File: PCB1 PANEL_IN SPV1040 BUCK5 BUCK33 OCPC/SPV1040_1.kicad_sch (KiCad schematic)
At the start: 14 parts, among them J2 SOLAR, U2 SPV1040TTR

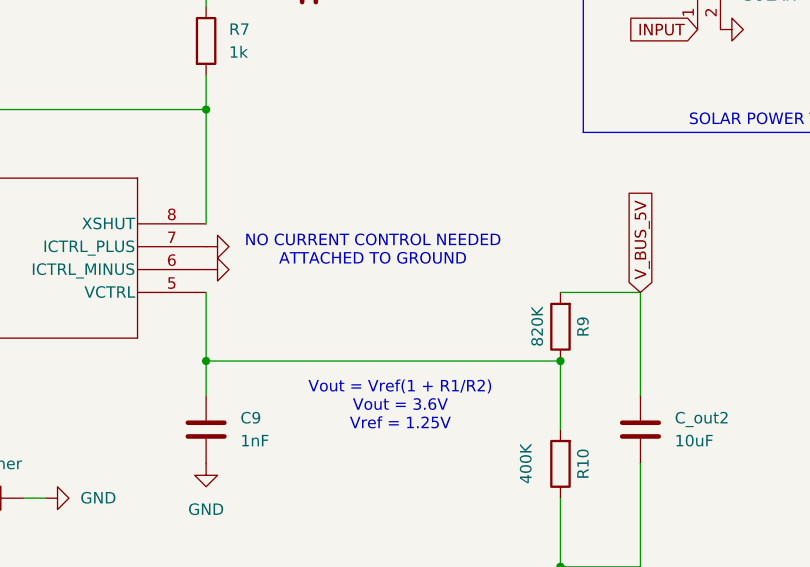
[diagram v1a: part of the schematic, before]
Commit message: Added some comments in POWERPCB, about bus interface
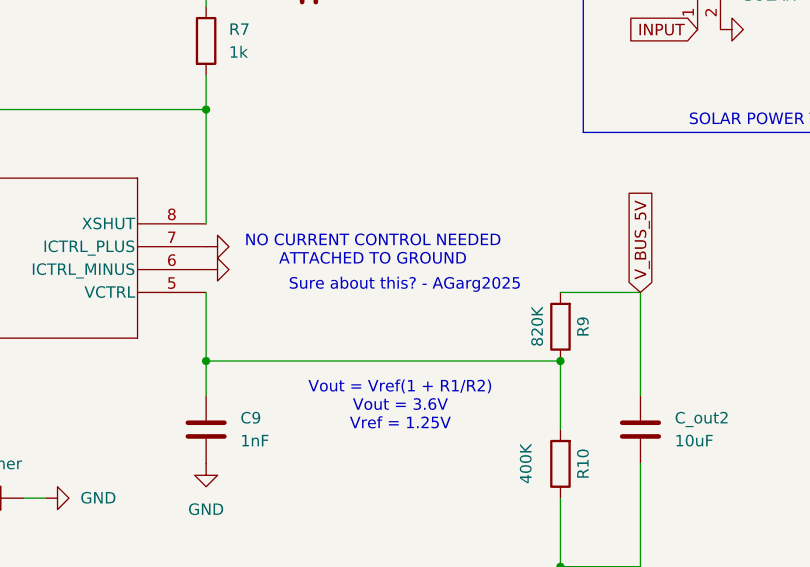
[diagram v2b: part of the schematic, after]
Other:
- note added: "Sure about this? - AGarg2025"
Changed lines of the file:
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@@
+		)
+	)
+	(text "Sure about this? - AGarg2025"
+		(exclude_from_sim no)
+		(at 147.828 71.628 0)
+		(effects
+			(font
+				(size 1.27 1.27)
+			)
 		)
 	)
@@
 	(label "BAT_MON+"
 		(at 234.95 68.58 0)
-		(fields_autoplaced yes)
 		(effects
 			(font
